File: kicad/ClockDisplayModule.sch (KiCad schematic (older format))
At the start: 5 parts, among them IC101 ATMEGA8-P, P101 CONN_01X05, P102 CONN_02X03

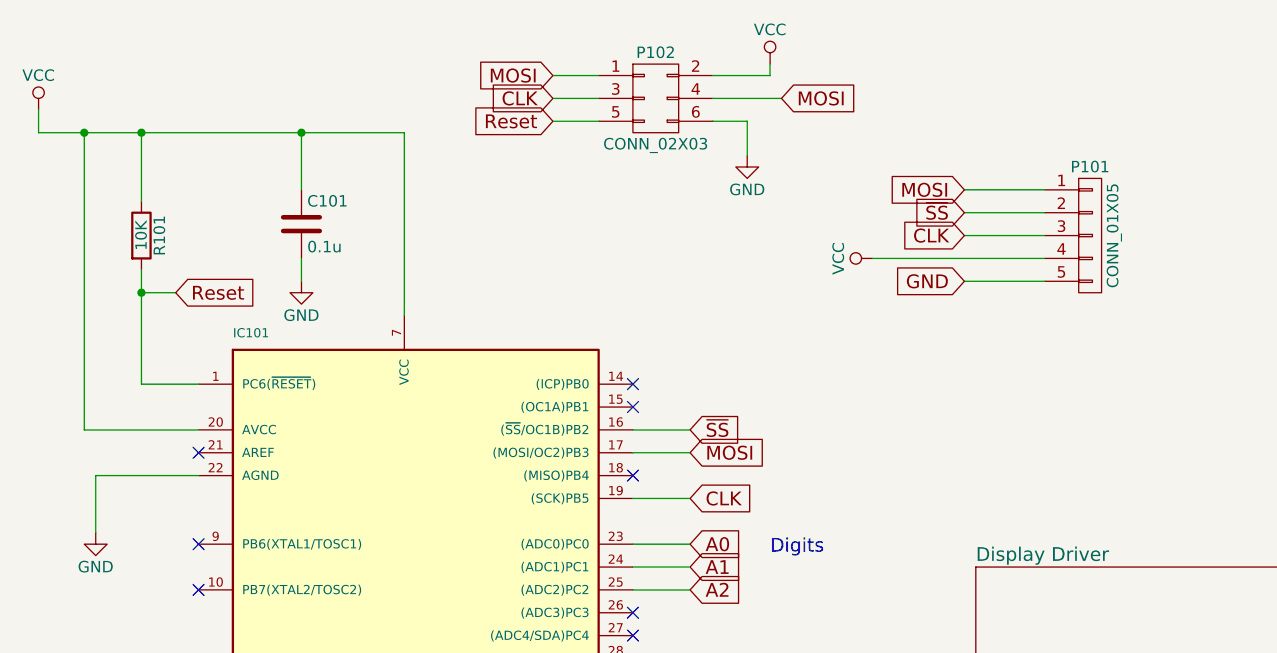
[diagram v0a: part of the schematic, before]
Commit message: Updated the layout for the controller side
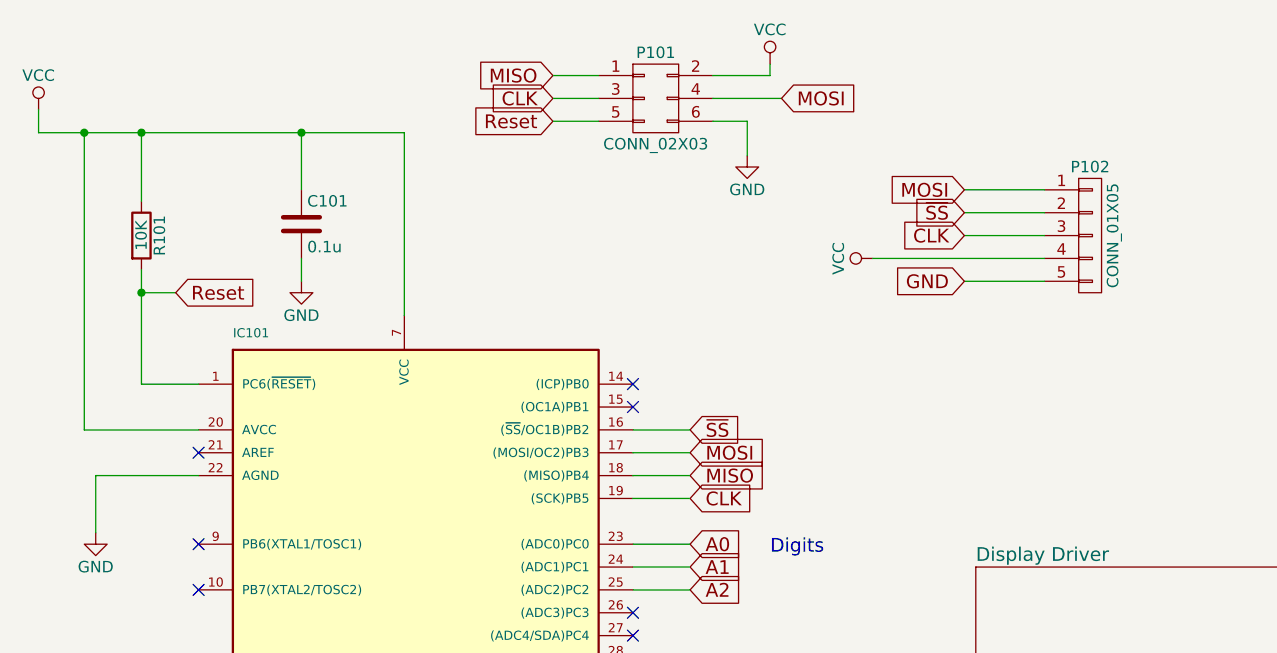
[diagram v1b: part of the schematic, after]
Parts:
- renumbered P102 to P101, P101 to P102
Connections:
- net MOSI: no longer P101.1 (P1)
- net MISO: now reaches IC101.18 ((MISO)PB4)
- net MISO: now also P101.1 (P1)
- no-connect marks 13 -> 12
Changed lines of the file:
@@
 D
 NoConn ~ 4750 4400
-$Comp
-L CONN_01X05 P101
-U 1 1 5575F20D
-P 6750 1650
-F 0 "P101" H 6750 1950 50  0000 C CNN
-F 1 "CONN_01X05" V 6850 1650 50  0000 C CNN
-F 2 "Pin_Headers:Pin_Header_Straight_1x05" H 6750 1650 60  0001 C CNN
-F 3 "" H 6750 1650 60  0000 C CNN
-	1    6750 1650
-	1    0    0    -1
-$EndComp
 Text GLabel 6200 1450 0    60   Input ~ 0
 MOSI
@@
 	4750 2500 5000 2500
 Wire Wire Line
-	2600 1800 2600 1900
-Wire Wire Line
-	2600 1900 2600 2300
+	2600 1800 2600 2300
 Wire Wire Line
 	2600 2300 2850 2300
 Wire Wire Line
-	2150 1200 2350 1200
-Wire Wire Line
-	2350 1200 2600 1200
-Wire Wire Line
-	2600 1200 3300 1200
-Wire Wire Line
-	3300 1200 3750 1200
+	2150 1200 3750 1200
 Wire Wire Line
 	3750 1200 3750 2000
@@
 NoConn ~ 4750 2400
 NoConn ~ 4750 2300
-NoConn ~ 4750 2700
 $Comp
 L GND #PWR03
@@
 NoConn ~ 2850 2600
 $Comp
-L CONN_02X03 P102
+L CONN_02X03 P101
 U 1 1 5589F70E
 P 4850 1050
-F 0 "P102" H 4850 1250 50  0000 C CNN
+F 0 "P101" H 4850 1250 50  0000 C CNN
 F 1 "CONN_02X03" H 4850 850 50  0000 C CNN
 F 2 "Pin_Headers:Pin_Header_Straight_2x03" H 4850 -150 60  0001 C CNN
@@
 $EndComp
 Text GLabel 4400 950  0    60   Input ~ 0
-MOSI
+MISO
 Text GLabel 4400 1050 0    60   Input ~ 0
 CLK
@@
 	2750 1900 2600 1900
 Connection ~ 2600 1900
+$Comp
+L CONN_01X05 P102
+U 1 1 5575F20D
+P 6750 1650
+F 0 "P102" H 6750 1950 50  0000 C CNN
+F 1 "CONN_01X05" V 6850 1650 50  0000 C CNN
+F 2 "Pin_Headers:Pin_Header_Straight_1x05" H 6750 1650 60  0001 C CNN
+F 3 "" H 6750 1650 60  0000 C CNN
+	1    6750 1650
+	1    0    0    -1
+$EndComp
+Text GLabel 5000 2700 2    60   Input ~ 0
+MISO
+Wire Wire Line
+	4750 2700 5000 2700
 $EndSCHEMATC

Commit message: Added some Conrad part numbers
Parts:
- P101: Conrad_PN (none) -> 741435 - 62
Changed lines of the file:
@@
 F 3 "" H 4850 -150 60  0000 C CNN
 F 4 "WS6G" H 4850 1050 60  0001 C CNN "MPN"
+F 5 " 741435 - 62 " H 4850 1050 60  0001 C CNN "Conrad_PN"
 	1    4850 1050
 	1    0    0    -1

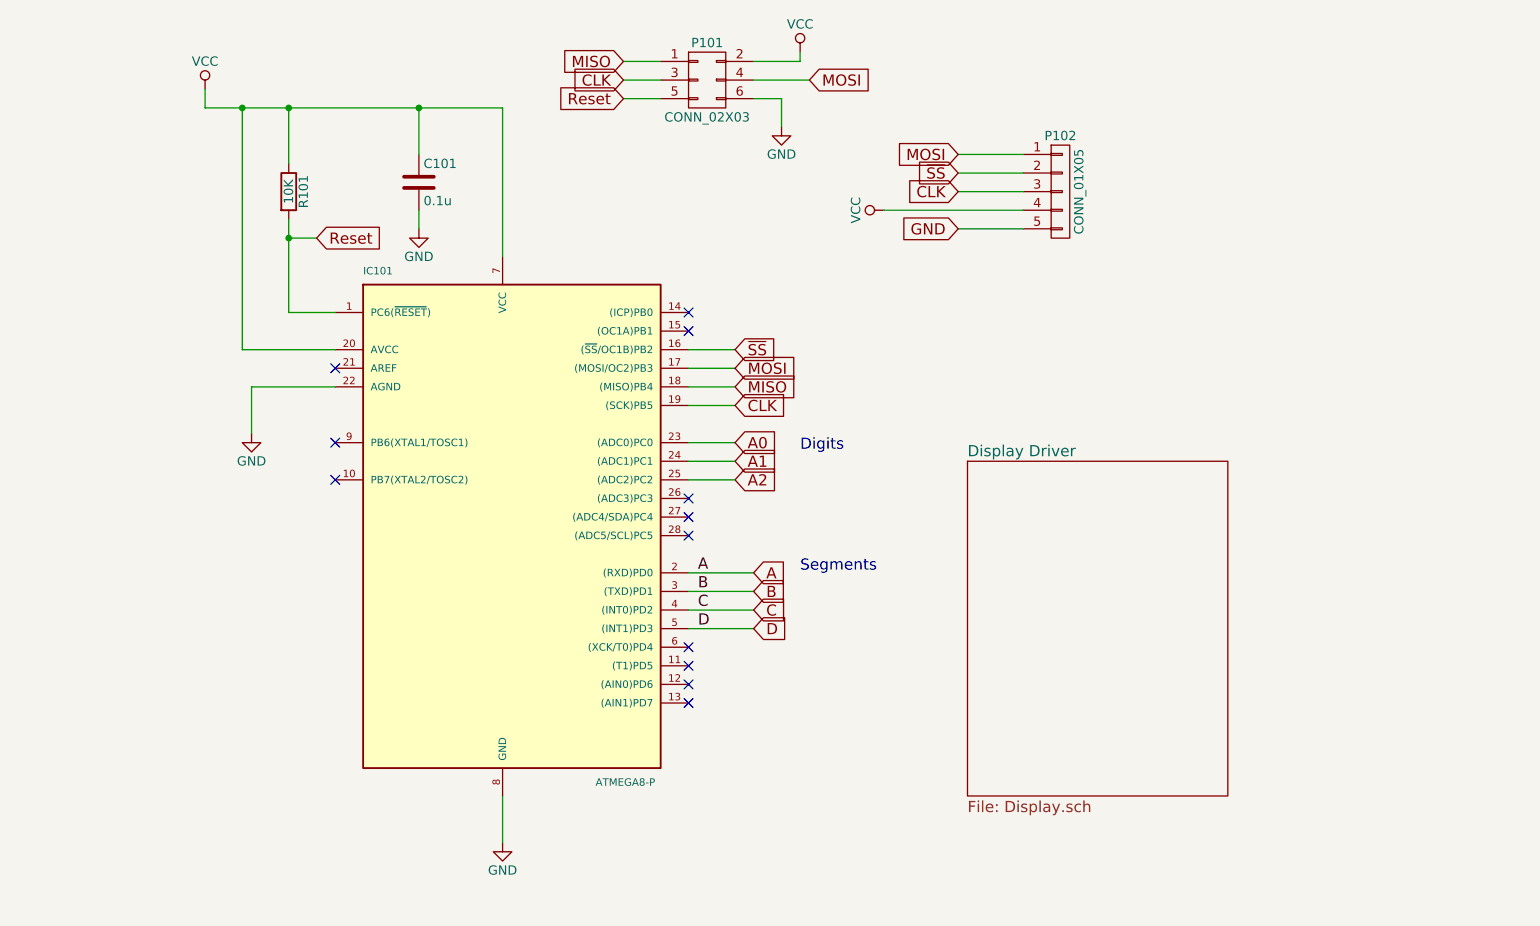
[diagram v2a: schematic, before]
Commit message: Correction to microcontroller footprint
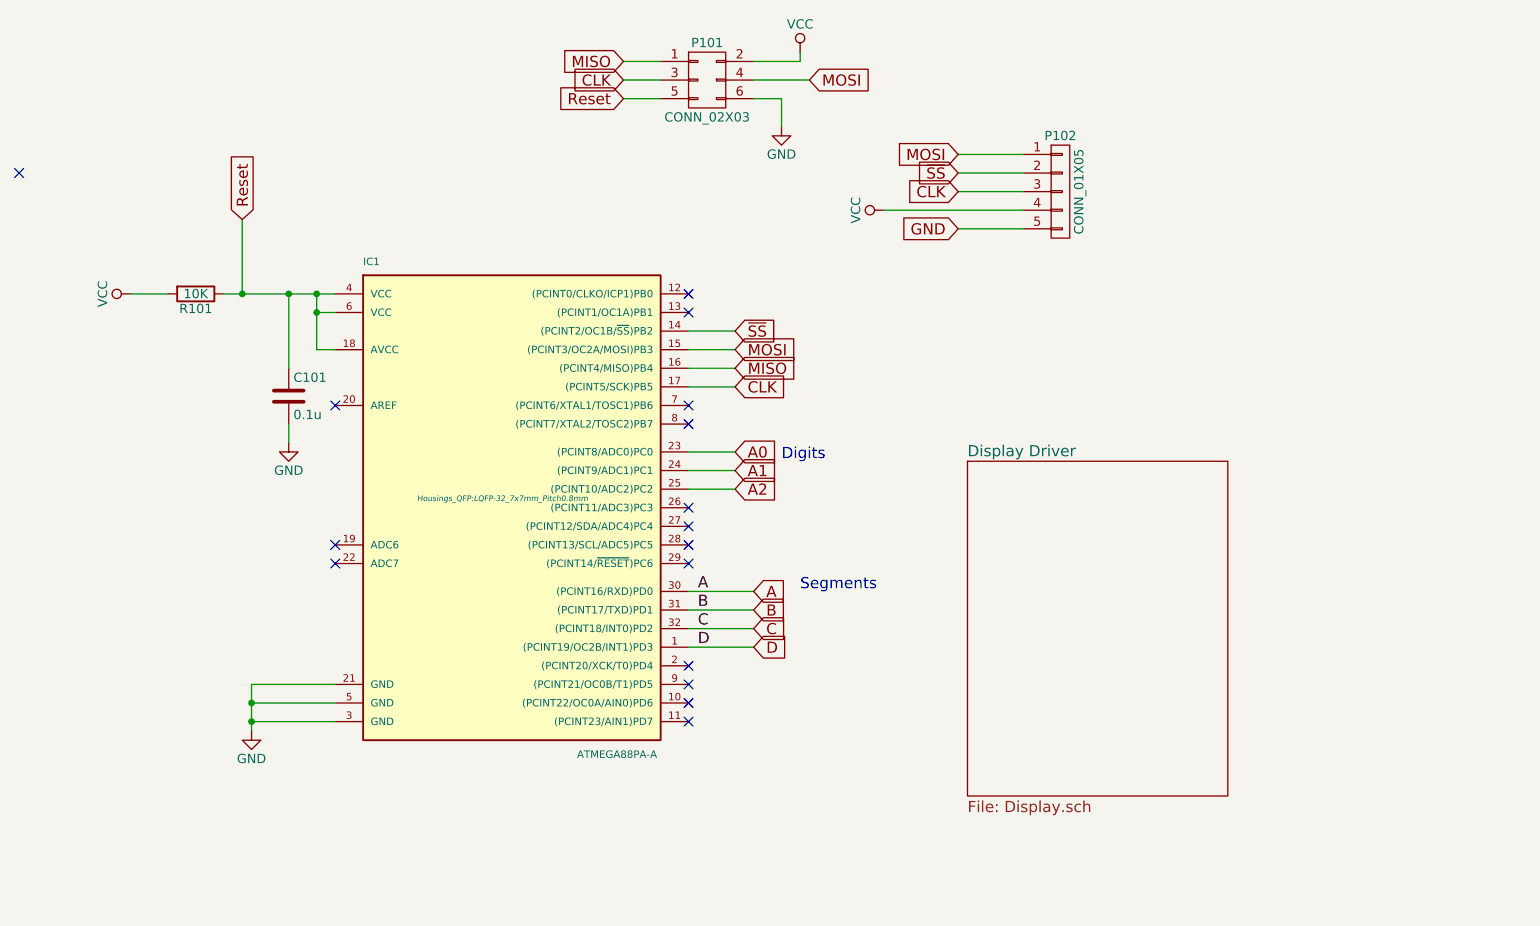
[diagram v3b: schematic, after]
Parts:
- removed IC101: ATMEGA8-P, Housings_QFP:TQFP-32_7x7mm_Pitch0.8mm, symbol ATMEGA8-P
- added IC1: ATMEGA88PA-A, Housings_QFP:LQFP-32_7x7mm_Pitch0.8mm, symbol ATMEGA88PA-A
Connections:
- net A: now also IC1.30 ((PCINT16/RXD)PD0)
- net A0: now also IC1.23 ((PCINT8/ADC0)PC0)
- net A1: now also IC1.24 ((PCINT9/ADC1)PC1)
- net A2: now also IC1.25 ((PCINT10/ADC2)PC2)
- net B: now also IC1.31 ((PCINT17/TXD)PD1)
- net C: now also IC1.32 ((PCINT18/INT0)PD2)
- net CLK: now also IC1.17 ((PCINT5/SCK)PB5)
- net D: now also IC1.1 ((PCINT19/OC2B/INT1)PD3)
- net GND: now also IC1.21 (GND), IC1.3 (GND), IC1.5 (GND)
- net MISO: now also IC1.16 ((PCINT4/MISO)PB4)
- net MOSI: now also IC1.15 ((PCINT3/OC2A/MOSI)PB3)
- net Reset: now also C101.1, R101.1, IC1.18 (AVCC), IC1.4 (VCC), IC1.6 (VCC); no longer R101.2
- net VCC: now also R101.2; no longer C101.1, R101.1
- net ~SS: now also IC1.14 ((PCINT2/OC1B/~SS~)PB2)
- no-connect marks 12 -> 16
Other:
- moved on the sheet: C101, R101
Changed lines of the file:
@@
 L R R101
 U 1 1 5575BA42
-P 2600 1650
-F 0 "R101" V 2680 1650 50  0000 C CNN
-F 1 "10K" V 2600 1650 50  0000 C CNN
-F 2 "Resistors_SMD:R_0805_HandSoldering" V 2530 1650 30  0001 C CNN
-F 3 "" H 2600 1650 30  0000 C CNN
-	1    2600 1650
-	1    0    0    -1
+P 2100 2200
+F 0 "R101" V 2180 2200 50  0000 C CNN
+F 1 "10K" V 2100 2200 50  0000 C CNN
+F 2 "Resistors_SMD:R_0805_HandSoldering" V 2030 2200 30  0001 C CNN
+F 3 "" H 2100 2200 30  0000 C CNN
+	1    2100 2200
+	0    1    1    0
 $EndComp
 $Comp
 L C C101
 U 1 1 5575BAA8
-P 3300 1600
-F 0 "C101" H 3325 1700 50  0000 L CNN
-F 1 "0.1u" H 3325 1500 50  0000 L CNN
-F 2 "Capacitors_SMD:C_0805_HandSoldering" H 3338 1450 30  0001 C CNN
-F 3 "" H 3300 1600 60  0000 C CNN
-	1    3300 1600
-	1    0    0    -1
-$EndComp
-$Comp
-L GND #PWR01
-U 1 1 5575BBAC
-P 3300 1850
-F 0 "#PWR01" H 3300 1600 50  0001 C CNN
-F 1 "GND" H 3300 1700 50  0000 C CNN
-F 2 "" H 3300 1850 60  0000 C CNN
-F 3 "" H 3300 1850 60  0000 C CNN
-	1    3300 1850
-	1    0    0    -1
-$EndComp
-Text GLabel 5000 2600 2    60   Input ~ 0
+P 2600 2750
+F 0 "C101" H 2625 2850 50  0000 L CNN
+F 1 "0.1u" H 2625 2650 50  0000 L CNN
+F 2 "Capacitors_SMD:C_0805_HandSoldering" H 2638 2600 30  0001 C CNN
+F 3 "" H 2600 2750 60  0000 C CNN
+	1    2600 2750
+	1    0    0    -1
+$EndComp
+Text GLabel 5000 2500 2    60   Input ~ 0
 MOSI
-Text GLabel 5000 2500 2    60   Input ~ 0
+Text GLabel 5000 2400 2    60   Input ~ 0
 ~SS
-Text GLabel 5000 2800 2    60   Input ~ 0
+Text GLabel 5000 2700 2    60   Input ~ 0
 CLK
-Text Label 4800 3700 0    60   ~ 0
+Text Label 4800 3800 0    60   ~ 0
 A
-Text Label 4800 3800 0    60   ~ 0
+Text Label 4800 3900 0    60   ~ 0
 B
-Text Label 4800 3900 0    60   ~ 0
+Text Label 4800 4000 0    60   ~ 0
 C
-Text Label 4800 4000 0    60   ~ 0
+Text Label 4800 4100 0    60   ~ 0
 D
 NoConn ~ 4750 4400
@@
 Text GLabel 6200 1850 0    60   Input ~ 0
 GND
-Wire Wire Line
-	4750 3700 5100 3700
-Wire Wire Line
-	4750 3800 5100 3800
-Wire Wire Line
-	4750 3900 5100 3900
-Wire Wire Line
-	4750 4000 5100 4000
-Wire Wire Line
-	6200 1450 6550 1450
-Wire Wire Line
-	6200 1550 6550 1550
-Wire Wire Line
-	6200 1650 6550 1650
-Wire Wire Line
-	5800 1750 6550 1750
-Wire Wire Line
-	6200 1850 6550 1850
-Wire Wire Line
-	5000 3000 4750 3000
-Wire Wire Line
-	5000 3100 4750 3100
-Wire Wire Line
-	4750 3200 5000 3200
-$Comp
-L ATMEGA8-P IC101
-U 1 1 5580770E
-P 3750 3400
-F 0 "IC101" H 3000 4700 40  0000 L BNN
-F 1 "ATMEGA8-P" H 4250 1950 40  0000 L BNN
-F 2 "Housings_QFP:TQFP-32_7x7mm_Pitch0.8mm" H 3750 3400 30  0001 C CIN
-F 3 "" H 3750 3400 60  0000 C CNN
-F 4 "ATMEGA88PV-10AUR" H 3750 3400 60  0001 C CNN "MPN"
-	1    3750 3400
-	1    0    0    -1
-$EndComp
-Wire Wire Line
-	4750 2800 5000 2800
-Wire Wire Line
-	4750 2600 5000 2600
-Wire Wire Line
-	4750 2500 5000 2500
-Wire Wire Line
-	2600 1800 2600 2300
-Wire Wire Line
-	2600 2300 2850 2300
-Wire Wire Line
-	2150 1200 3750 1200
-Wire Wire Line
-	3750 1200 3750 2000
-Wire Wire Line
-	3300 1200 3300 1450
-Connection ~ 3300 1200
-Wire Wire Line
-	3300 1750 3300 1850
-Wire Wire Line
-	2600 1500 2600 1200
-Connection ~ 2600 1200
-$Comp
-L GND #PWR02
-U 1 1 558085AA
-P 3750 5150
-F 0 "#PWR02" H 3750 4900 50  0001 C CNN
-F 1 "GND" H 3750 5000 50  0000 C CNN
-F 2 "" H 3750 5150 60  0000 C CNN
-F 3 "" H 3750 5150 60  0000 C CNN
-	1    3750 5150
-	1    0    0    -1
-$EndComp
-Wire Wire Line
-	3750 4900 3750 5150
-NoConn ~ 2850 3200
-NoConn ~ 2850 3000
-NoConn ~ 4750 2400
-NoConn ~ 4750 2300
-$Comp
-L GND #PWR03
+$Comp
+L GND #PWR01
 U 1 1 558087E3
-P 2400 2950
-F 0 "#PWR03" H 2400 2700 50  0001 C CNN
-F 1 "GND" H 2400 2800 50  0000 C CNN
-F 2 "" H 2400 2950 60  0000 C CNN
-F 3 "" H 2400 2950 60  0000 C CNN
-	1    2400 2950
-	1    0    0    -1
-$EndComp
-Wire Wire Line
-	2850 2700 2400 2700
-Wire Wire Line
-	2400 2700 2400 2950
-Wire Wire Line
-	2850 2500 2350 2500
-Wire Wire Line
-	2350 2500 2350 1200
-Connection ~ 2350 1200
-$Comp
-L VCC #PWR04
+P 2400 4550
+F 0 "#PWR01" H 2400 4300 50  0001 C CNN
+F 1 "GND" H 2400 4400 50  0000 C CNN
+F 2 "" H 2400 4550 60  0000 C CNN
+F 3 "" H 2400 4550 60  0000 C CNN
+	1    2400 4550
+	1    0    0    -1
+$EndComp
+$Comp
+L VCC #PWR02
 U 1 1 558686BB
-P 2150 1100
-F 0 "#PWR04" H 2150 950 50  0001 C CNN
-F 1 "VCC" H 2150 1250 50  0000 C CNN
-F 2 "" H 2150 1100 60  0000 C CNN
-F 3 "" H 2150 1100 60  0000 C CNN
-	1    2150 1100
-	1    0    0    -1
-$EndComp
-Wire Wire Line
-	2150 1200 2150 1100
-$Comp
-L VCC #PWR05
+P 1750 2200
+F 0 "#PWR02" H 1750 2050 50  0001 C CNN
+F 1 "VCC" H 1750 2350 50  0000 C CNN
+F 2 "" H 1750 2200 60  0000 C CNN
+F 3 "" H 1750 2200 60  0000 C CNN
+	1    1750 2200
+	0    -1   -1   0
+$EndComp
+$Comp
+L VCC #PWR03
 U 1 1 5586896F
 P 5800 1750
-F 0 "#PWR05" H 5800 1600 50  0001 C CNN
+F 0 "#PWR03" H 5800 1600 50  0001 C CNN
 F 1 "VCC" H 5800 1900 50  0000 C CNN
 F 2 "" H 5800 1750 60  0000 C CNN
@@
 	0    -1   -1   0
 $EndComp
-Text GLabel 5100 3700 2    60   Input ~ 0
+Text GLabel 5100 3800 2    60   Input ~ 0
 A
-Text GLabel 5100 3800 2    60   Input ~ 0
+Text GLabel 5100 3900 2    60   Input ~ 0
 B
-Text GLabel 5100 3900 2    60   Input ~ 0
+Text GLabel 5100 4000 2    60   Input ~ 0
 C
-Text GLabel 5100 4000 2    60   Input ~ 0
+Text GLabel 5100 4100 2    60   Input ~ 0
 D
-NoConn ~ 4750 4100
 NoConn ~ 4750 4200
 NoConn ~ 4750 4300
-Text GLabel 5000 3000 2    60   Input ~ 0
+Text GLabel 5000 3050 2    60   Input ~ 0
 A0
-Text GLabel 5000 3100 2    60   Input ~ 0
+Text GLabel 5000 3150 2    60   Input ~ 0
 A1
-Text GLabel 5000 3200 2    60   Input ~ 0
+Text GLabel 5000 3250 2    60   Input ~ 0
 A2
 $Sheet
@@
 F1 "Display.sch" 60
 $EndSheet
-Text Notes 5350 3050 0    60   ~ 0
+Text Notes 5250 3100 0    60   ~ 0
 Digits
-Text Notes 5350 3700 0    60   ~ 0
+Text Notes 5350 3800 0    60   ~ 0
 Segments
-NoConn ~ 4750 3300
-NoConn ~ 4750 3400
-NoConn ~ 4750 3500
-NoConn ~ 2850 2600
 $Comp
 L CONN_02X03 P101
@@
 CLK
 $Comp
-L VCC #PWR06
+L VCC #PWR04
 U 1 1 5589F87B
 P 5350 900
-F 0 "#PWR06" H 5350 750 50  0001 C CNN
+F 0 "#PWR04" H 5350 750 50  0001 C CNN
 F 1 "VCC" H 5350 1050 50  0000 C CNN
 F 2 "" H 5350 900 60  0000 C CNN
@@
 	1    0    0    -1
 $EndComp
-Wire Wire Line
-	5350 900  5350 950
-Wire Wire Line
-	5350 950  5100 950
 Text GLabel 5400 1050 2    60   Input ~ 0
 MOSI
 $Comp
-L GND #PWR07
+L GND #PWR05
 U 1 1 5589F8CC
 P 5250 1300
-F 0 "#PWR07" H 5250 1050 50  0001 C CNN
+F 0 "#PWR05" H 5250 1050 50  0001 C CNN
 F 1 "GND" H 5250 1150 50  0000 C CNN
 F 2 "" H 5250 1300 60  0000 C CNN
@@
 	1    0    0    -1
 $EndComp
-Wire Wire Line
-	5100 1150 5250 1150
-Wire Wire Line
-	5250 1150 5250 1300
-Wire Wire Line
-	5100 1050 5400 1050
-Wire Wire Line
-	4600 950  4400 950
-Wire Wire Line
-	4600 1050 4400 1050
 Text GLabel 4400 1150 0    60   Input ~ 0
 Reset
-Wire Wire Line
-	4400 1150 4600 1150
-Text GLabel 2750 1900 2    60   Input ~ 0
+Text GLabel 2350 1800 1    60   Input ~ 0
 Reset
-Wire Wire Line
-	2750 1900 2600 1900
-Connection ~ 2600 1900
 $Comp
 L CONN_01X05 P102
@@
 	1    0    0    -1
 $EndComp
-Text GLabel 5000 2700 2    60   Input ~ 0
+Text GLabel 5000 2600 2    60   Input ~ 0
 MISO
+$Comp
+L ATMEGA88PA-A IC1
+U 1 1 55B13D6F
+P 3750 3300
+F 0 "IC1" H 3000 4550 40  0000 L BNN
+F 1 "ATMEGA88PA-A" H 4150 1900 40  0000 L BNN
+F 2 "Housings_QFP:LQFP-32_7x7mm_Pitch0.8mm" H 3750 3300 30  0000 C CIN
+F 3 "" H 3750 3300 60  0000 C CNN
+	1    3750 3300
+	1    0    0    -1
+$EndComp
+NoConn ~ 4750 4500
+Wire Wire Line
+	4750 3800 5100 3800
+Wire Wire Line
+	4750 3900 5100 3900
+Wire Wire Line
+	4750 4000 5100 4000
+Wire Wire Line
+	4750 4100 5100 4100
+Wire Wire Line
+	6200 1450 6550 1450
+Wire Wire Line
+	6200 1550 6550 1550
+Wire Wire Line
+	6200 1650 6550 1650
+Wire Wire Line
+	5800 1750 6550 1750
+Wire Wire Line
+	6200 1850 6550 1850
+Wire Wire Line
+	5000 3050 4750 3050
+Wire Wire Line
+	5000 3150 4750 3150
+Wire Wire Line
+	4750 3250 5000 3250
 Wire Wire Line
 	4750 2700 5000 2700
+Wire Wire Line
+	4750 2500 5000 2500
+Wire Wire Line
+	4750 2400 5000 2400
+Wire Wire Line
+	2850 4300 2400 4300
+Wire Wire Line
+	2400 4300 2400 4550
+Wire Wire Line
+	5350 900  5350 950
+Wire Wire Line
+	5350 950  5100 950
+Wire Wire Line
+	5100 1150 5250 1150
+Wire Wire Line
+	5250 1150 5250 1300
+Wire Wire Line
+	5100 1050 5400 1050
+Wire Wire Line
+	4600 950  4400 950
+Wire Wire Line
+	4600 1050 4400 1050
+Wire Wire Line
+	4400 1150 4600 1150
+Wire Wire Line
+	4750 2600 5000 2600
+Wire Wire Line
+	2850 4400 2400 4400
+Connection ~ 2400 4400
+Wire Wire Line
+	2850 4500 2400 4500
+Connection ~ 2400 4500
+$Comp
+L GND #PWR06
+U 1 1 5575BBAC
+P 2600 3000
+F 0 "#PWR06" H 2600 2750 50  0001 C CNN
+F 1 "GND" H 2600 2850 50  0000 C CNN
+F 2 "" H 2600 3000 60  0000 C CNN
+F 3 "" H 2600 3000 60  0000 C CNN
+	1    2600 3000
+	1    0    0    -1
+$EndComp
+Wire Wire Line
+	2600 2900 2600 3000
+Wire Wire Line
+	2750 2200 2750 2500
+Wire Wire Line
+	2750 2300 2850 2300
+Connection ~ 2750 2200
+Wire Wire Line
+	1750 2200 1950 2200
+Wire Wire Line
+	2250 2200 2850 2200
+Wire Wire Line
+	2750 2500 2850 2500
+Connection ~ 2750 2300
+Wire Wire Line
+	2600 2600 2600 2200
+Connection ~ 2600 2200
+Wire Wire Line
+	2350 1800 2350 2200
+Connection ~ 2350 2200
+NoConn ~ 2850 2800
+NoConn ~ 4750 2200
+NoConn ~ 4750 2300
+NoConn ~ 4750 2800
+NoConn ~ 4750 2900
+NoConn ~ 2850 3550
+NoConn ~ 2850 3650
+NoConn ~ 4750 3350
+NoConn ~ 4750 3450
+NoConn ~ 4750 3550
+NoConn ~ 4750 3650
+NoConn ~ 1150 1550
 $EndSCHEMATC
